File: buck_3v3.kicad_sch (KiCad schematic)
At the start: 16 parts, among them U3 XTPS564257DRLR

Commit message: CuPhy: adding ports
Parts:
- removed R10: 20K, Resistor_SMD:R_0805_2012Metric_Pad1.20x1.40mm_HandSolder, symbol Device:R
- removed R9: 47K, Resistor_SMD:R_0805_2012Metric_Pad1.20x1.40mm_HandSolder, symbol Device:R
- renumbered C67 to C86, C69 to C87, C26 to C88, C68 to C89, C71 to C90, C72 to C91, C73 to C92, L3 to L6, R11 to R23, R12 to R24, TP7 to TP16, TP8 to TP17, TP9 to TP18, U3 to U6

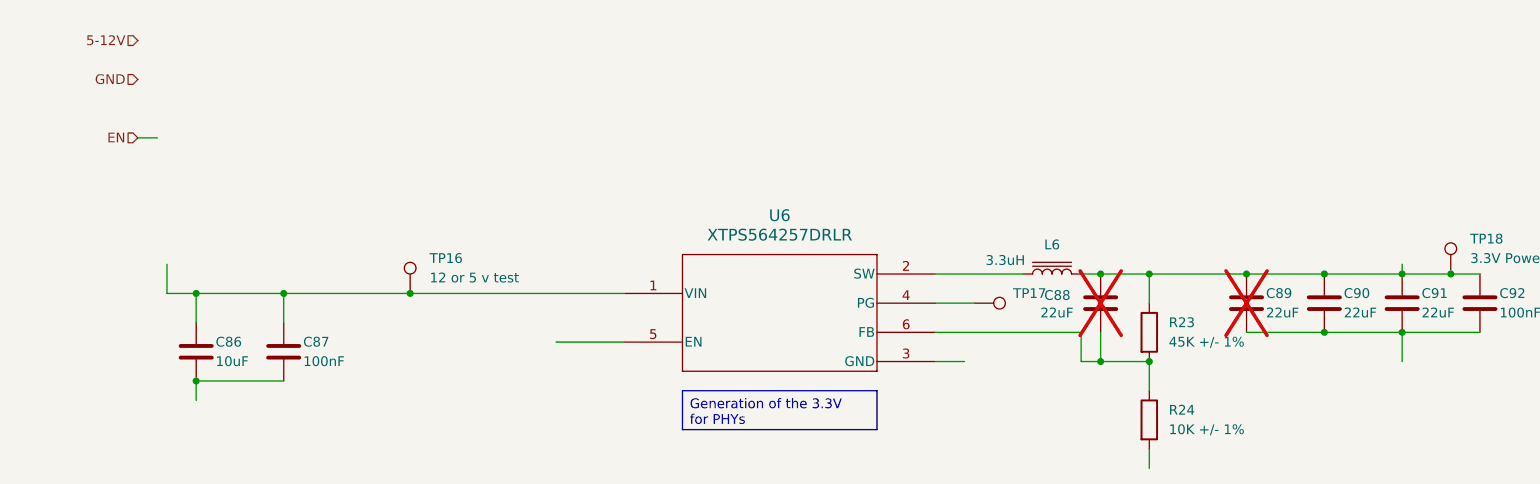
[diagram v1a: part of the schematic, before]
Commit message: schematics: fixing the voltage rail and updating the files
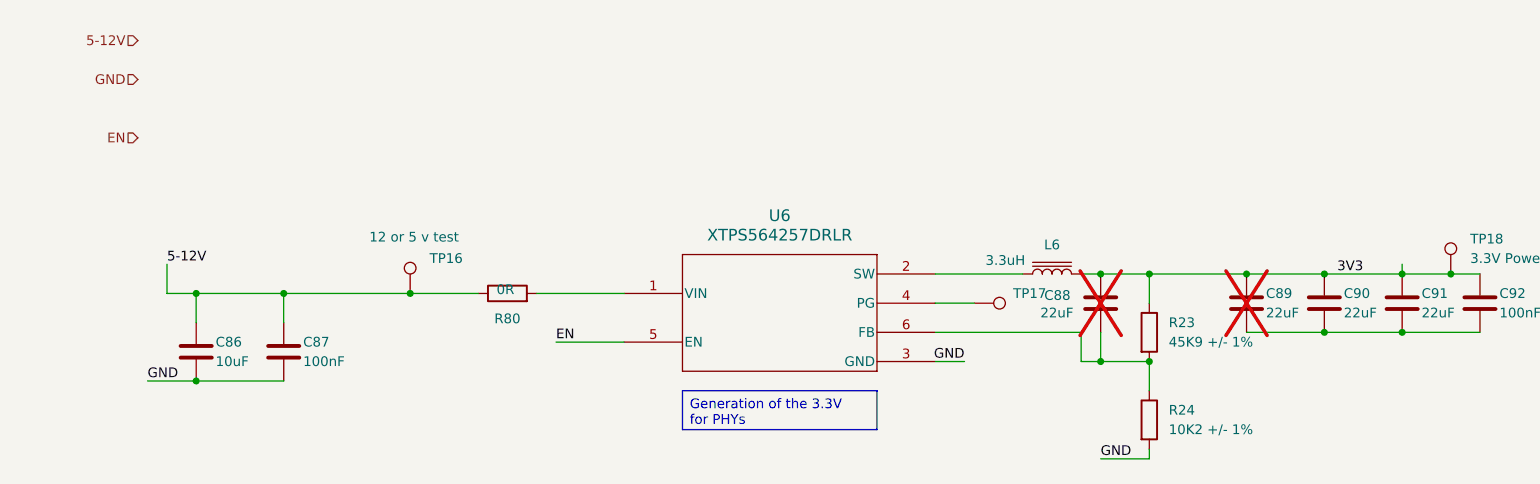
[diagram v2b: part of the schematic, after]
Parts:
- added R80: 0R, KL_Footprints:R_2512, symbol KL_R:R_0R_2W_5_2512
- R23: value 45K +/- 1% -> 45K9 +/- 1%
- R24: value 10K +/- 1% -> 10K2 +/- 1%
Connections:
- net 3V3: now also C88.1, C89.1, C90.1, C91.1, C92.1, L6.2, R23.1, TP18.1
- net 5-12V: now also C86.1, C87.1, TP16.1, R80.1
- net EN: now also U6.5 (EN)
- net GND: now also C86.2, C87.2, R24.2, U6.3 (GND)
- new net: R80.2, U6.1 (VIN)

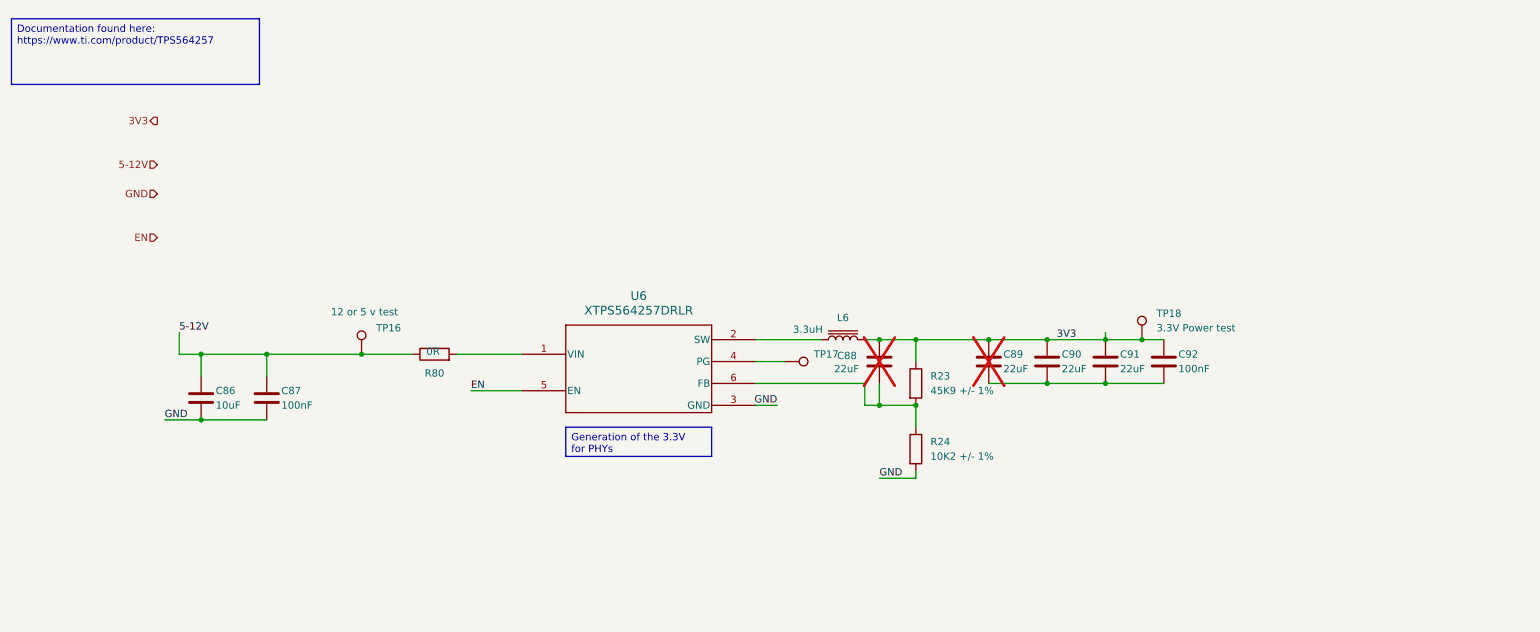
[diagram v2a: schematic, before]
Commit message: switch: finished 1st version
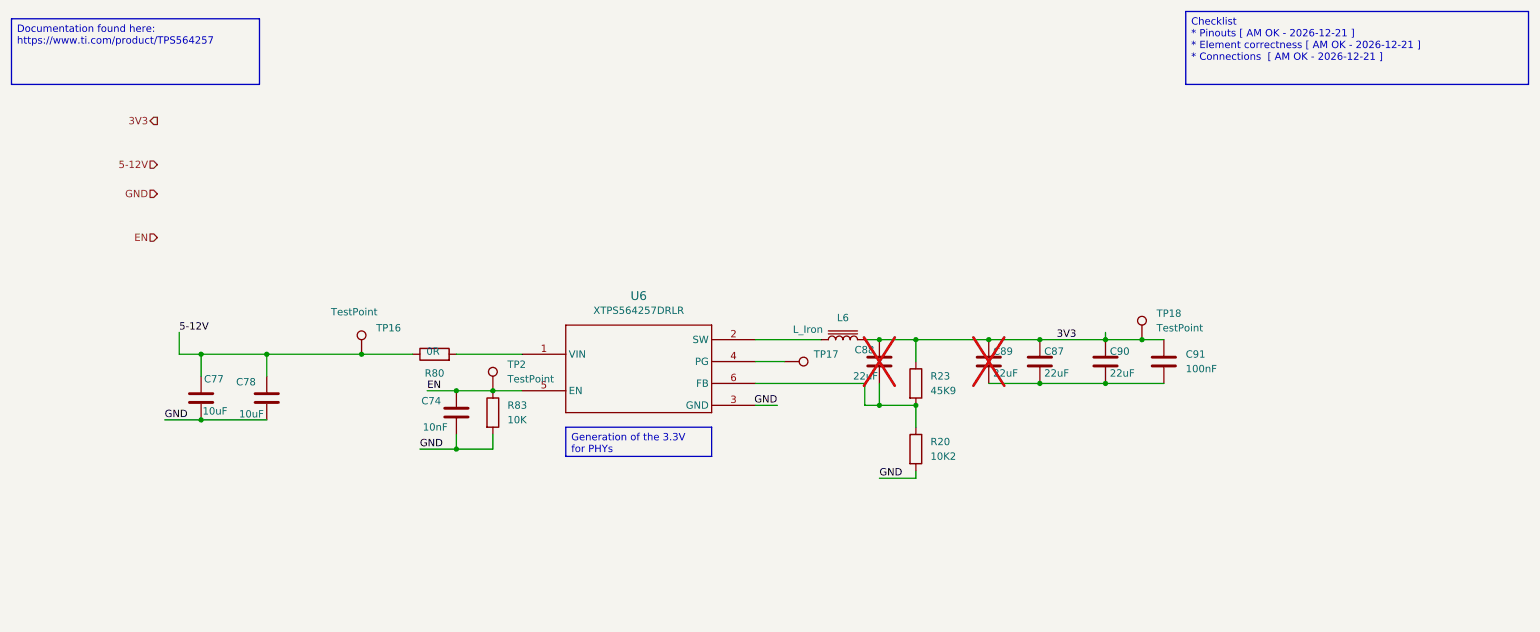
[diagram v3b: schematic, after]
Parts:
- removed C86: 10uF, Capacitor_SMD:C_0805_2012Metric_Pad1.18x1.45mm_HandSolder, symbol Device:C
- removed C87, C92: 100nF, Capacitor_SMD:C_0805_2012Metric_Pad1.18x1.45mm_HandSolder, symbol Device:C
- removed C88, C89, C90, C91: 22uF, Capacitor_SMD:C_0805_2012Metric_Pad1.18x1.45mm_HandSolder, symbol Device:C
- removed R23: 45K9 +/- 1%, Resistor_SMD:R_0805_2012Metric_Pad1.20x1.40mm_HandSolder, symbol Device:R
- removed R24: 10K2 +/- 1%, Resistor_SMD:R_0805_2012Metric_Pad1.20x1.40mm_HandSolder, symbol Device:R
- removed U6: XTPS564257DRLR, TPS564242DRLR_TEX, symbol tps5642:XTPS564257DRLR
- added C74: 10nF, KL:C_0603, symbol KL_C:C_10nF_25V_X7R_0603_20
- added C77, C78: 10uF, KL:C_0603, symbol KL_C:C_10uF_25V_X5R_0603_20
- added C87, C88, C89, C90: 22uF, KL:C_0603, symbol KL_C:C_22uF_10V_X5R_0603_20
- added C91: 100nF, KL:C_0603, symbol KL_C:C_100nF_10V_X7R_0603_10
- added R20: 10K2, KL:R_0603, symbol KL_R:R_10K2_100mW_1_0603
- added R23: 45K9, KL:R_0603, symbol KL_R:R_45K9_125mW_1_0603
- added R83: 10K, KL:R_0603, symbol KL_R:R_10K_100mW_5_0603
- added TP2: TestPoint, symbol Connector:TestPoint
- added U6: XTPS564257DRLR, KL:SOT-563, symbol KL_IC_Power:TI_TPS564357DRLR
- L6: value 3.3uH -> L_Iron
- TP16: value 12 or 5 v test -> TestPoint
- TP17: value 12v test -> TestPoint
- TP18: value 3.3V Power test -> TestPoint
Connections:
- net 3V3: now also C87.1, C88.1, C89.1, C90.1, C91.1, R23.1
- net 5-12V: now also C77.1, C78.1
- net EN: now also C74.1, R83.1, TP2.1, U6.5 (EN)
- net GND: now also C74.2, C77.2, C78.2, R20.2, R83.2, U6.3 (GND)
- net at L6.1: now also U6.2 (SW)
- net at R80.2: now also U6.1 (VIN)
- net at TP17.1: now also U6.4 (PG)
- new net: C88.2, R20.1, R23.2, U6.6 (FB)
- new net: C87.2, C89.2, C90.2, C91.2
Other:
- company: (none) -> Kebag-Logic <contact@kebag-logic.com>
- title: (none) -> Switch 3V3 Power Rail

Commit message: minor footprint fixing
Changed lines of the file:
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@@
 		(fields_autoplaced yes)
 		(property "Reference" "TP17"
-			(at 157.48 74.9299 90)
+			(at 157.48 76.1999 90)
 			(effects
 				(font
@@
 			)
 		)
-		(property "Datasheet" "https://www.ti.com/lit/gpn/tps564257"
+		(property "Datasheet" ""
 			(at 127 72.39 0)
 			(effects

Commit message: review of +3V3 converter
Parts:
- removed C78: 10uF, KL:C_0603, symbol KL_C:C_10uF_25V_X5R_0603_20
- removed C88: 22uF, KL:C_0603, symbol KL_C:C_22uF_10V_X5R_0603_20
- removed L6: L_Iron, symbol Device:L_Iron
- removed TP16, TP17, TP18, TP2: TestPoint, symbol Connector:TestPoint
- added C78: 100nF, KL:C_0603, symbol KL_C:C_100nF_16V_X7R_0603_10
- added C88: 10pF, Capacitor_SMD:C_0201_0603Metric, symbol KL_C:C_10pF_25V_C0G_0603_5
- added C94: 10uF, KL:C_0603, symbol KL_C:C_10uF_25V_X5R_0603_20
- added L1: 3u3, KL:L_3u3_EXLA1V0603, symbol KL_L:L_3u3_8A
- added R94: 10K, KL_Footprints:C_0603, symbol KL_R:R_10K_100mW_5_0603
- added TP16, TP17, TP18, TP2: ~, Connector_PinHeader_2.54mm:PinHeader_1x01_P2.54mm_Vertical, symbol KL_TP:TestPoint
- C74, C77, R83: now not fitted; now left out of the parts list
- C89: now left out of the parts list
- U6: value XTPS564257DRLR -> TPS564257DRLR
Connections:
- net 5-12V: no longer C77.1
- net EN: now also TP2.1
- net GND: now also C87.2, C89.2, C90.2, C91.2, C78.2, C94.2
- net at U6.2 (SW): now also L1.1
- net at R20.1, R23.2, U6.6 (FB): now also C88.2
- net at U6.4 (PG): now also R94.1, TP17.1
- net at R80.2, U6.1 (VIN): now also C77.1, C78.1, C94.1, TP16.1
- net 3V3 renamed +3V3
- net +3V3: now also C88.1, L1.2, R94.2, TP18.1
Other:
- note added: "Based on WEBENCH design: https://drive.google.com/file/d/1exyRvEr94bITdX-GvbbsN41mesaBmIx9/view?usp=drive_link"
- note added: "Not sure if debounce is necessary. Current resistor assumes pull-up for EN?"
- moved on the sheet: C87, C89, C90, C91, R20, R23, R80
